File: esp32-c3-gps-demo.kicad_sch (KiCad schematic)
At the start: 50 parts, among them J1 USB_C_Receptacle_USB2.0_16P, SW1 SW_Push, SW2 SW_Push, U1 TPS54331, U2 ESP32-C3-WROOM-02, U3 SRV05-4, U4 W25Q128JVS, U5 L96-M33

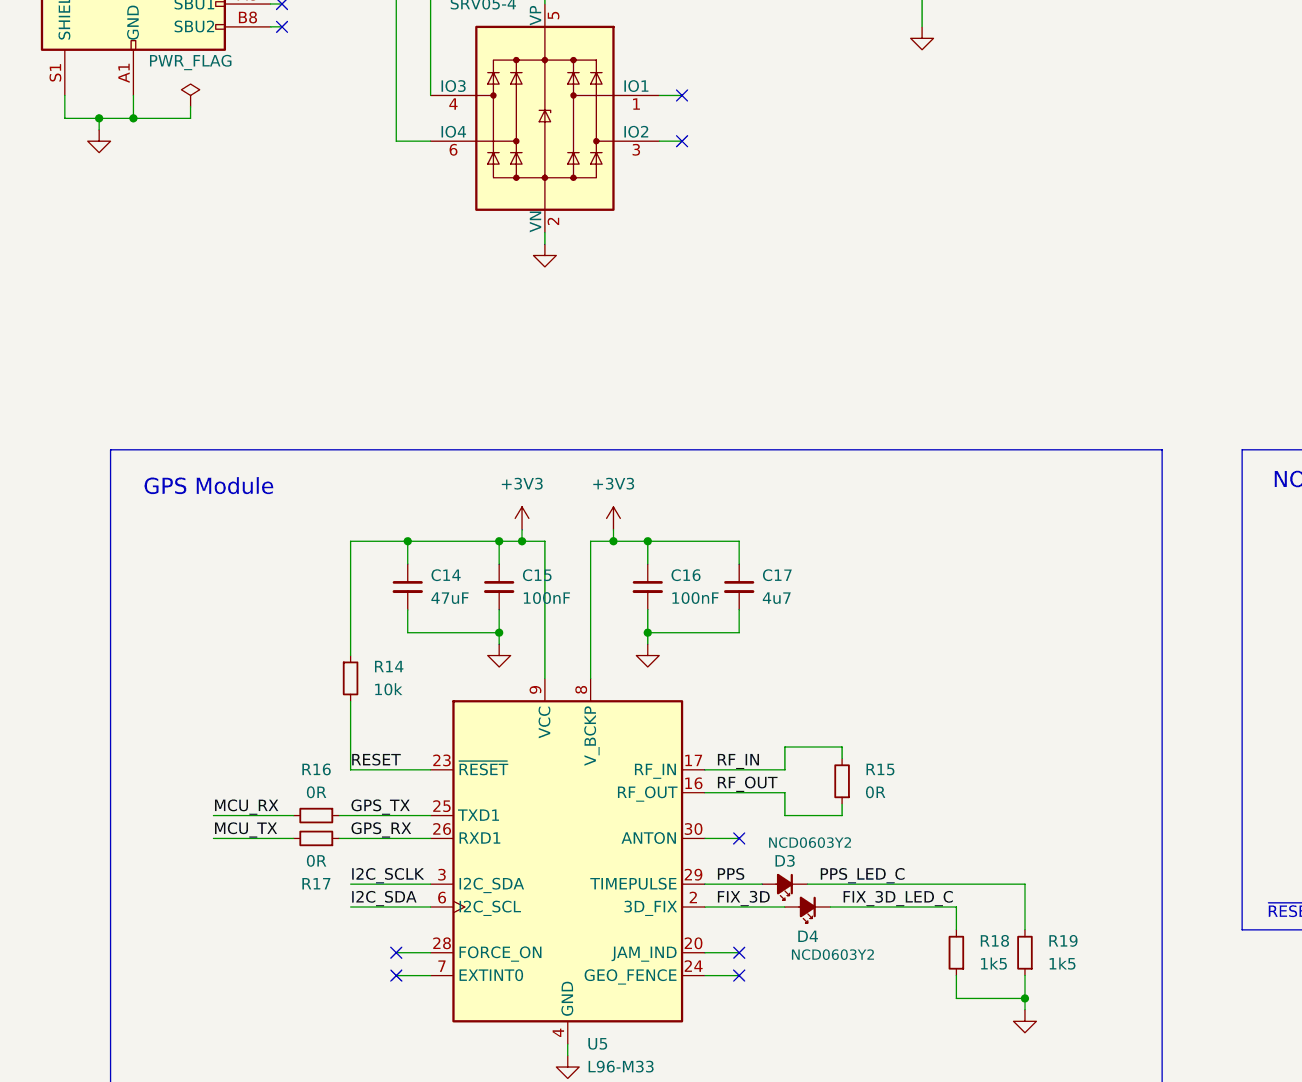
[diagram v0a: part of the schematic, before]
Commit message: Work in progress.  Put down a mag sensor and EEPROM in schematic, but parts not finalized
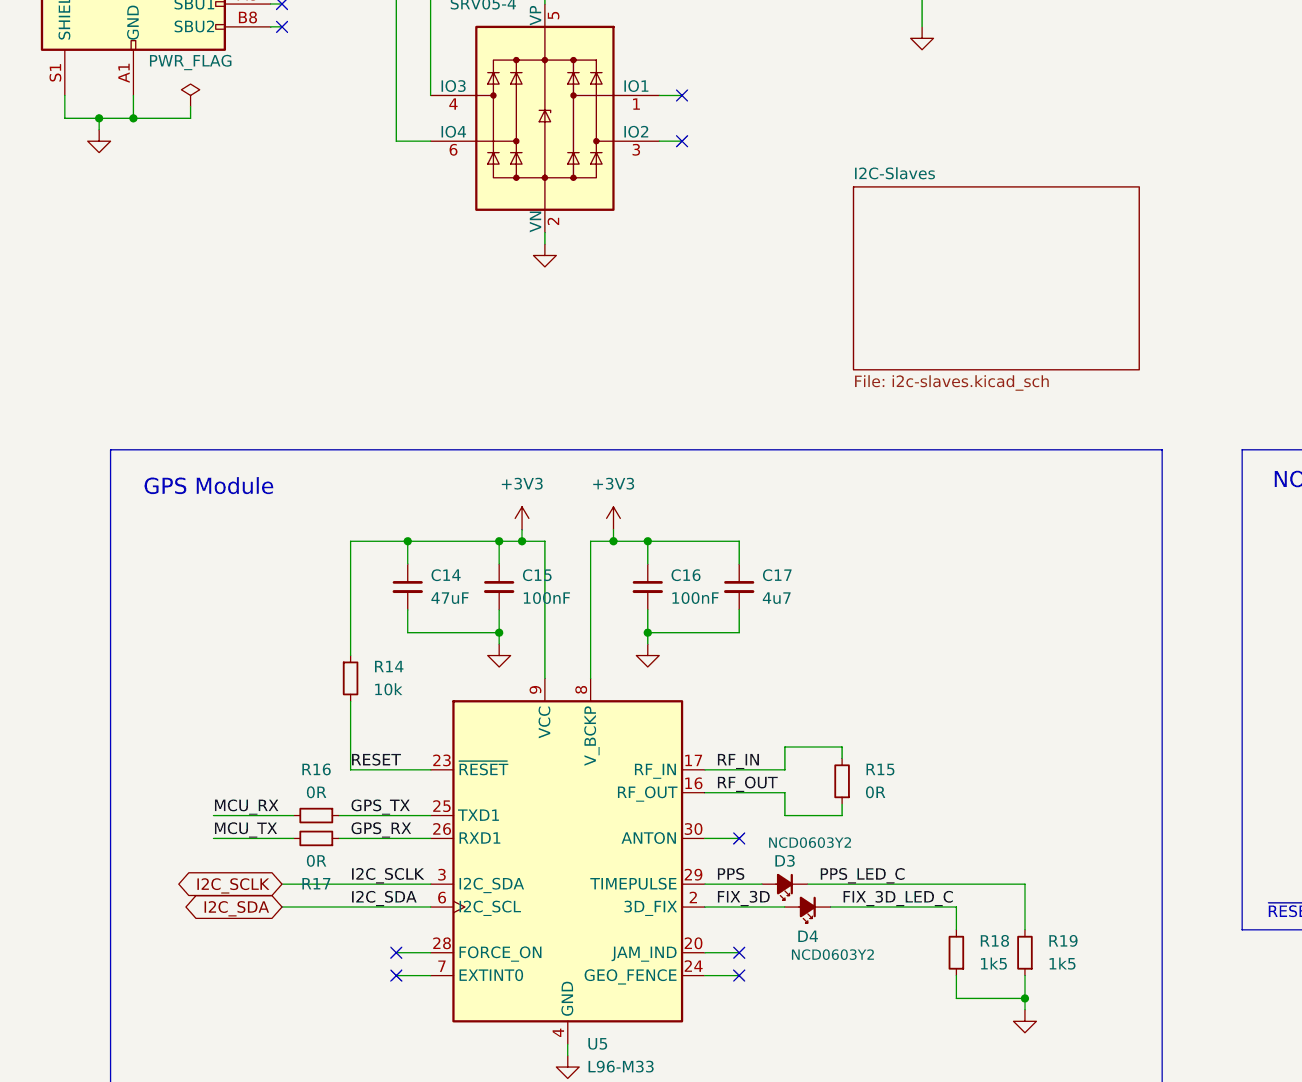
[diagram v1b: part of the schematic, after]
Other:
- added sheet I2C-Slaves (i2c-slaves.kicad_sch)
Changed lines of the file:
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@@
 	(wire
 		(pts
-			(xy 53.34 158.75) (xy 62.23 158.75)
-		)
-		(stroke
-			(width 0)
-			(type default)
-		)
-	)
-	(wire
-		(pts
 			(xy 236.22 31.75) (xy 236.22 29.21)
 		)
@@
 	(wire
 		(pts
+			(xy 45.72 156.21) (xy 62.23 156.21)
+		)
+		(stroke
+			(width 0)
+			(type default)
+		)
+	)
+	(wire
+		(pts
 			(xy 210.82 64.77) (xy 222.25 64.77)
 		)
@@
 	(wire
 		(pts
+			(xy 45.72 158.75) (xy 62.23 158.75)
+		)
+		(stroke
+			(width 0)
+			(type default)
+		)
+	)
+	(wire
+		(pts
 			(xy 223.52 53.34) (xy 226.06 53.34)
 		)
@@
 	(wire
 		(pts
-			(xy 53.34 156.21) (xy 62.23 156.21)
-		)
-		(stroke
-			(width 0)
-			(type default)
-		)
-	)
-	(wire
-		(pts
 			(xy 210.82 67.31) (xy 210.82 64.77)
 		)
@@
 		)
 	)
+	(global_label "I2C_SCLK"
+		(shape bidirectional)
+		(at 45.72 156.21 180)
+		(fields_autoplaced yes)
+		(effects
+			(font
+				(size 1.27 1.27)
+			)
+			(justify right)
+		)
+		(property "Intersheetrefs" "${INTERSHEET_REFS}"
+			(at 32.794 156.21 0)
+			(effects
+				(font
+					(size 1.27 1.27)
+				)
+				(justify right)
+				(hide yes)
+			)
+		)
+	)
+	(global_label "I2C_SDA"
+		(shape bidirectional)
+		(at 45.72 158.75 180)
+		(fields_autoplaced yes)
+		(effects
+			(font
+				(size 1.27 1.27)
+			)
+			(justify right)
+		)
+		(property "Intersheetrefs" "${INTERSHEET_REFS}"
+			(at 34.0035 158.75 0)
+			(effects
+				(font
+					(size 1.27 1.27)
+				)
+				(justify right)
+				(hide yes)
+			)
+		)
+	)
 	(symbol
 		(lib_name "GND_1")
@@
 				)
 			)
+		)
+	)
+	(sheet
+		(at 109.22 78.74)
+		(size 31.75 20.32)
+		(exclude_from_sim no)
+		(in_bom yes)
+		(on_board yes)
+		(dnp no)
+		(fields_autoplaced yes)
+		(stroke
+			(width 0.1524)
+			(type solid)
+		)
+		(fill
+			(color 0 0 0 0.0000)
+		)
+		(property "Sheetname" "I2C-Slaves"
+			(at 109.22 78.0284 0)
+			(effects
+				(font
+					(size 1.27 1.27)
+				)
+				(justify left bottom)
+			)
+		)
+		(property "Sheetfile" "i2c-slaves.kicad_sch"
+			(at 109.22 99.6446 0)
+			(effects
+				(font
+					(size 1.27 1.27)
+				)
+				(justify left top)
+			)
+		)
+		(instances
+			(project "esp32-c3-gps-demo"
+				(path "/381d9348-5880-4d6e-bf80-1347922c9fad"
+					(page "2")
+				)
+			)

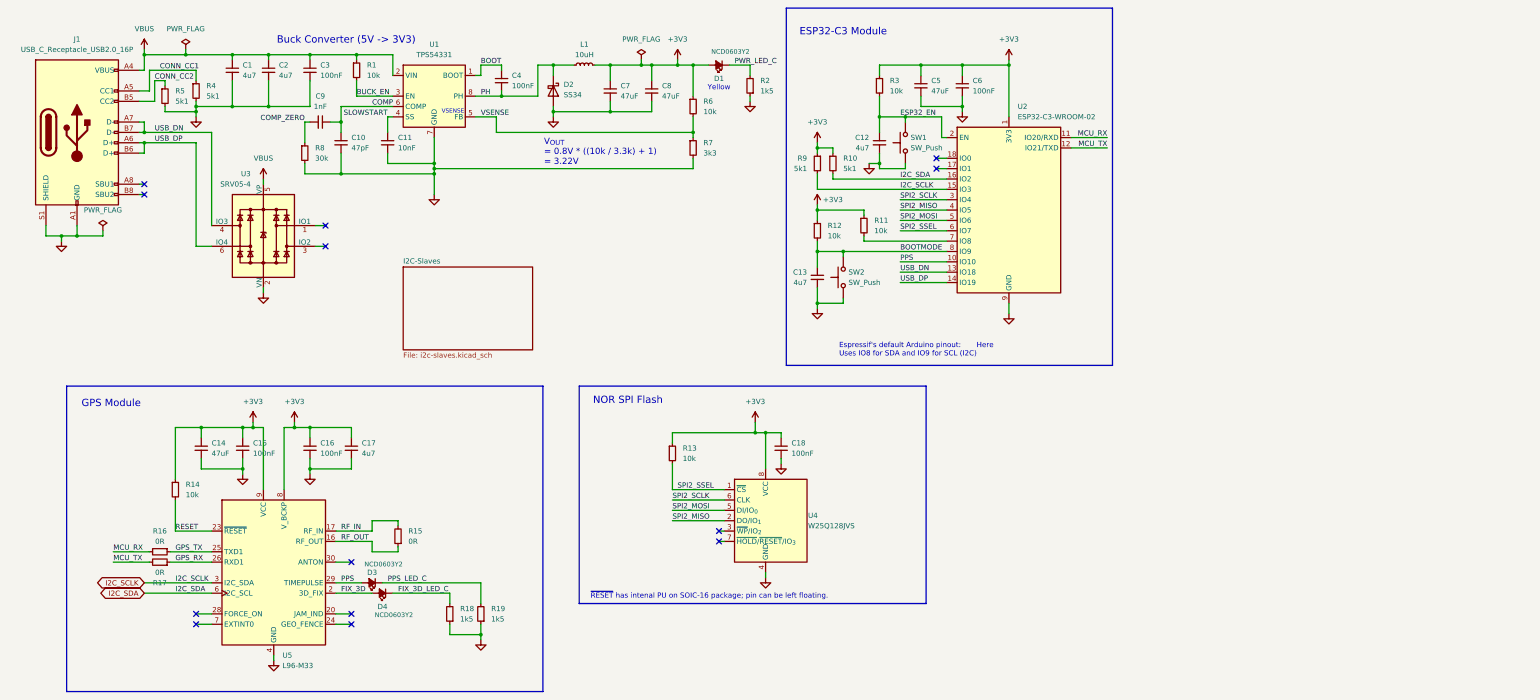
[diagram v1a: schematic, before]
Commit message: Put down an LIS3DH on the schematic without connections so as not to forget to use the accel
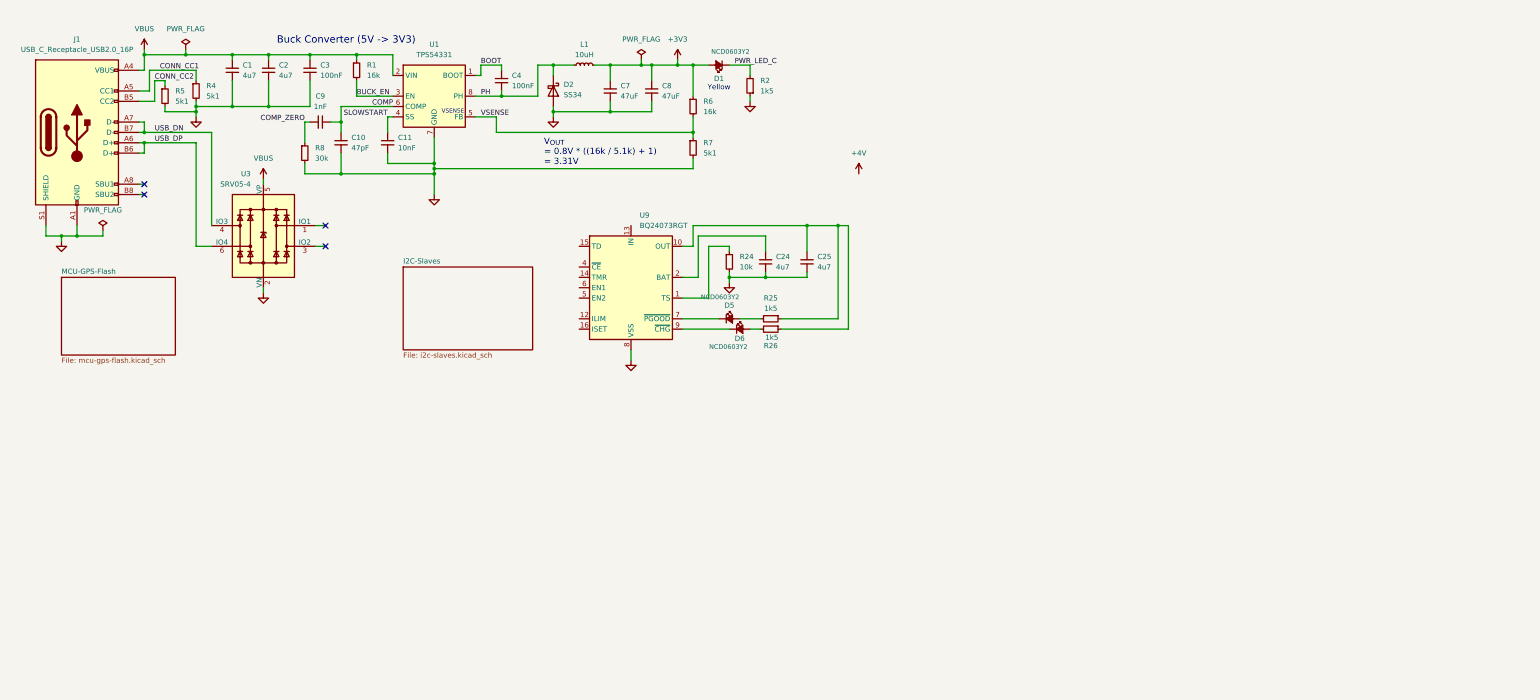
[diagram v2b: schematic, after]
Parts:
- removed C12, C13, C17: 4u7, Capacitor_SMD:C_0603_1608Metric, symbol Device:C_Small
- removed C14, C5: 47uF, Capacitor_SMD:C_0805_2012Metric, symbol Device:C_Small
- removed C15, C16, C18, C6: 100nF, Capacitor_SMD:C_0603_1608Metric, symbol Device:C_Small
- removed D3, D4: NCD0603Y2, LED_SMD:LED_0603_1608Metric, symbol Device:LED_Small_Filled
- removed R10, R9: 5k1, Resistor_SMD:R_0603_1608Metric, symbol Device:R_Small
- removed R11, R12, R13, R14, R3: 10k, Resistor_SMD:R_0603_1608Metric, symbol Device:R_Small
- removed R15, R16, R17: 0R, Resistor_SMD:R_0603_1608Metric, symbol Device:R_Small
- removed R18, R19: 1k5, Resistor_SMD:R_0603_1608Metric, symbol Device:R_Small
- removed SW1, SW2: SW_Push, Button_Switch_SMD:SW_Push_1P1T_XKB_TS-1187A, symbol Switch:SW_Push
- removed U2: ESP32-C3-WROOM-02, esp32-c3-gps-demo:ESP32-C3-WROOM-02_NoVias, symbol RF_Module:ESP32-C3-WROOM-02
- removed U4: W25Q128JVS, Package_SO:SOIC-8_5.23x5.23mm_P1.27mm, symbol Memory_Flash:W25Q128JVS
- removed U5: L96-M33, RF_GPS:Quectel_L96, symbol esp32-c3-gps-demo:L96-M33
- added C24, C25: 4u7, Capacitor_SMD:C_0603_1608Metric, symbol Device:C_Small
- added D5, D6: NCD0603Y2, LED_SMD:LED_0603_1608Metric, symbol Device:LED_Small_Filled
- added R24: 10k, Resistor_SMD:R_0603_1608Metric, symbol Device:R_Small
- added R25, R26: 1k5, Resistor_SMD:R_0603_1608Metric, symbol Device:R_Small
- added U9: BQ24073RGT, Package_DFN_QFN:VQFN-16-1EP_3x3mm_P0.5mm_EP1.6x1.6mm, symbol Battery_Management:BQ24073RGT
- R1, R6: value 10k -> 16k; footprint Resistor_SMD:R_0603_1608Metric -> Resistor_SMD:R_0805_2012Metric; LCSC Part # C25804 -> C17490; Manufacturer Part Number 0603WAF1002T5E -> 0805W8F1602T5E; Power 100mW -> 125mW; Voltage 75V -> 150V
- R7: value 3k3 -> 5k1; LCSC Part # C22978 -> C23186; Manufacturer Part Number 0603WAF3301T5E -> 0603WAF5101T5E
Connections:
- net GND: now also C24.2, C25.2, R24.2, U9.17 (VSS), U9.8 (VSS)
- new net: C25.1, R25.1, R26.1, U9.10 (OUT), U9.11 (OUT)
- new net: C24.1, U9.2 (BAT), U9.3 (BAT)
- new net: D6.1 (K), U9.9 (~{CHG})
- new net: D6.2 (A), R26.2
- new net: D5.2 (A), R25.2
- new net: R24.1, U9.1 (TS)
- new net: D5.1 (K), U9.7 (~{PGOOD})
- no-connect marks 13 -> 4
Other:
- added sheet MCU-GPS-Flash (mcu-gps-flash.kicad_sch)
- note added: "V_{OUT} = 0.8V * ((16k / 5.1k) + 1) = 3.31V"
- note removed: "ESP32-C3 Module"
- note removed: "Espressif's default Arduino pinout: Uses IO8 for SDA and IO9 for SCL (I2C)"
- note removed: "GPS Module"
- note removed: "Here"
- note removed: "NOR SPI Flash"
- note removed: "V_{OUT} = 0.8V * ((10k / 3.3k) + 1) = 3.22V"
- note removed: "~{RESET} has intenal PU on SOIC-16 package; pin can be left floating."

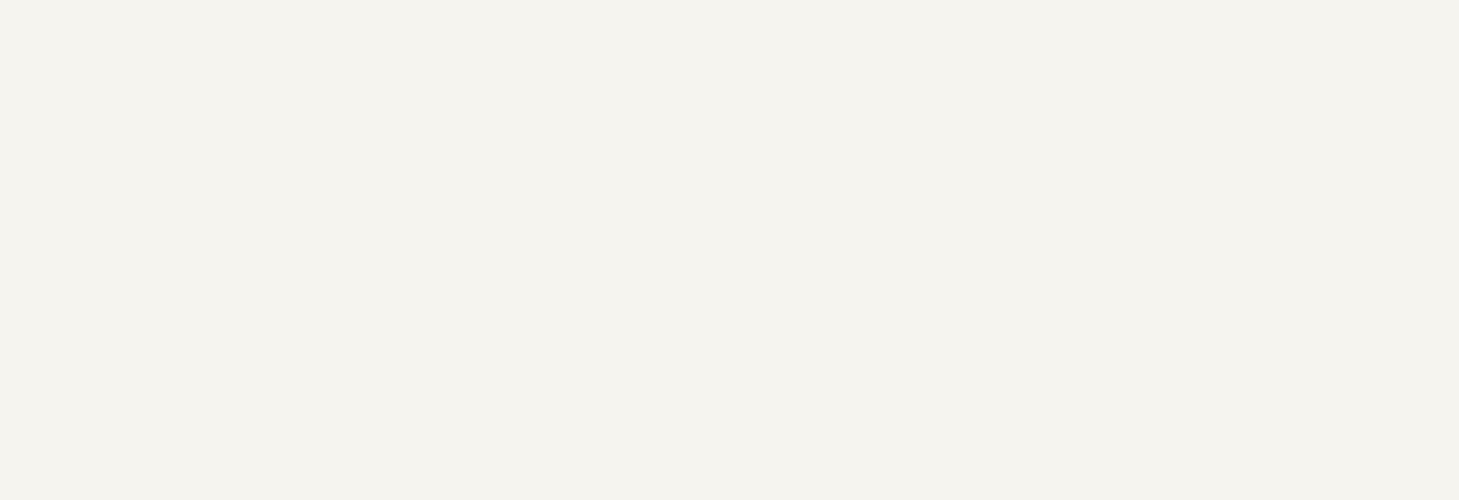
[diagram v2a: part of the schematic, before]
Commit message: Started adding battery circuitry to power the board from 1.5V.  Added symbol and footprints for alternate magnetometer and GNSS modules
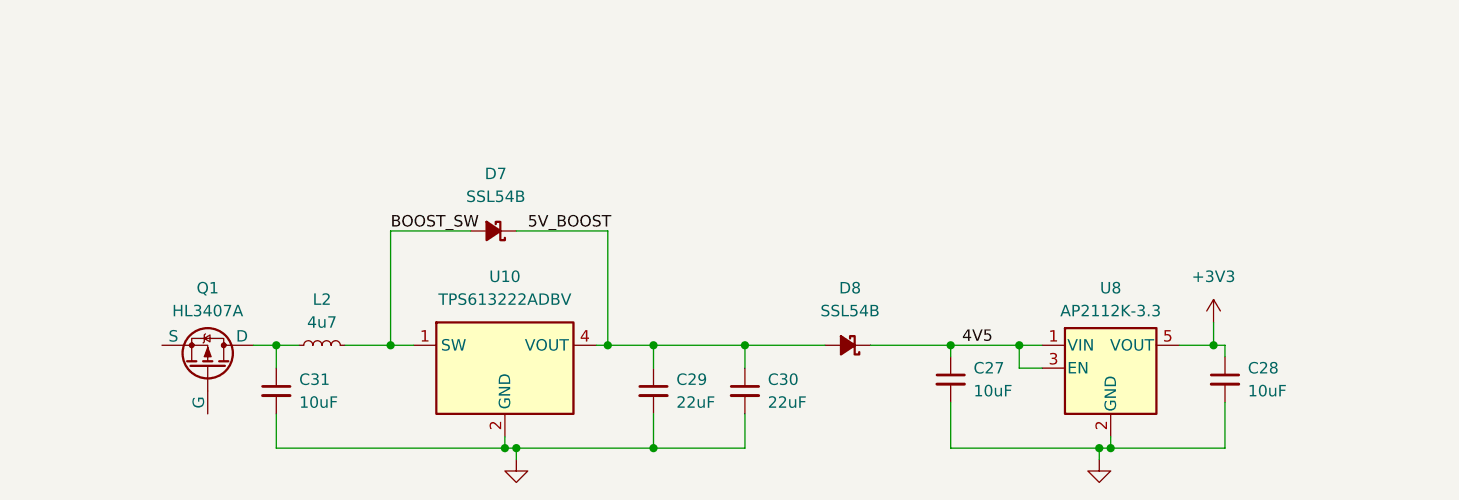
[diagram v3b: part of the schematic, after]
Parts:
- added C27, C28, C31: 10uF, Capacitor_SMD:C_0603_1608Metric, symbol Device:C_Small
- added C29, C30: 22uF, Capacitor_SMD:C_0805_2012Metric, symbol Device:C_Small
- added D7, D8: SSL54B, Diode_SMD:D_SMB, symbol Device:D_Schottky_Small_Filled
- added L2: 4u7, Inductor_SMD:L_Sunlord_SWPA6045S, symbol Device:L_Small
- added Q1: HL3407A, Package_TO_SOT_SMD:SOT-23, symbol Simulation_SPICE:PMOS
- added U10: TPS613222ADBV, Package_TO_SOT_SMD:SOT-23-5, symbol Regulator_Switching:TPS613222ADBV
- added U8: AP2112K-3.3, Package_TO_SOT_SMD:SOT-23-5, symbol Regulator_Linear:AP2112K-3.3
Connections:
- net +3V3: now also C28.1, U8.5 (VOUT)
- net GND: now also C27.2, C28.2, C29.2, C30.2, C31.2, U10.2 (GND), U8.2 (GND)
- new net: C31.1, L2.1, Q1.1 (D)
- new net 4V5: C27.1, D8.1 (K), U8.1 (VIN), U8.3 (EN)
- new net 5V_BOOST: C29.1, C30.1, D7.1 (K), D8.2 (A), U10.4 (VOUT)
- new net BOOST_SW: D7.2 (A), L2.2, U10.1 (SW)
